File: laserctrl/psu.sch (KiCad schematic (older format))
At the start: 30 parts, among them U1 MC34063

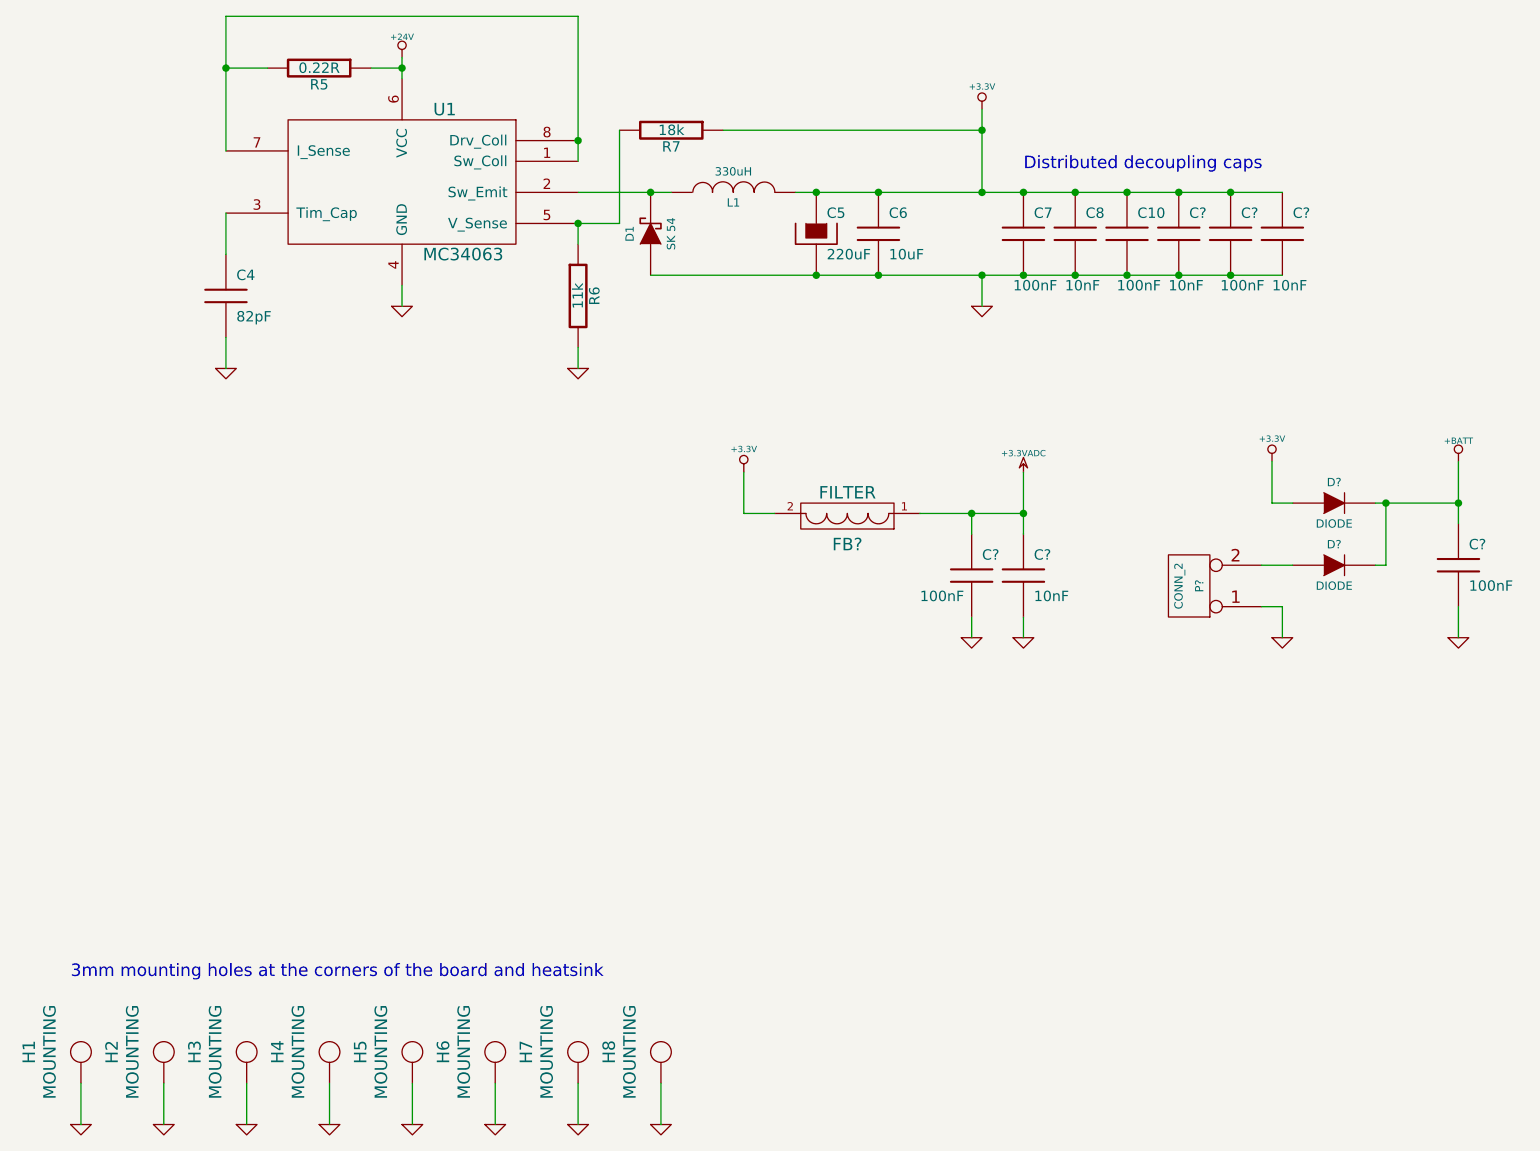
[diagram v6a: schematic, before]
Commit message: Added NTC sensors
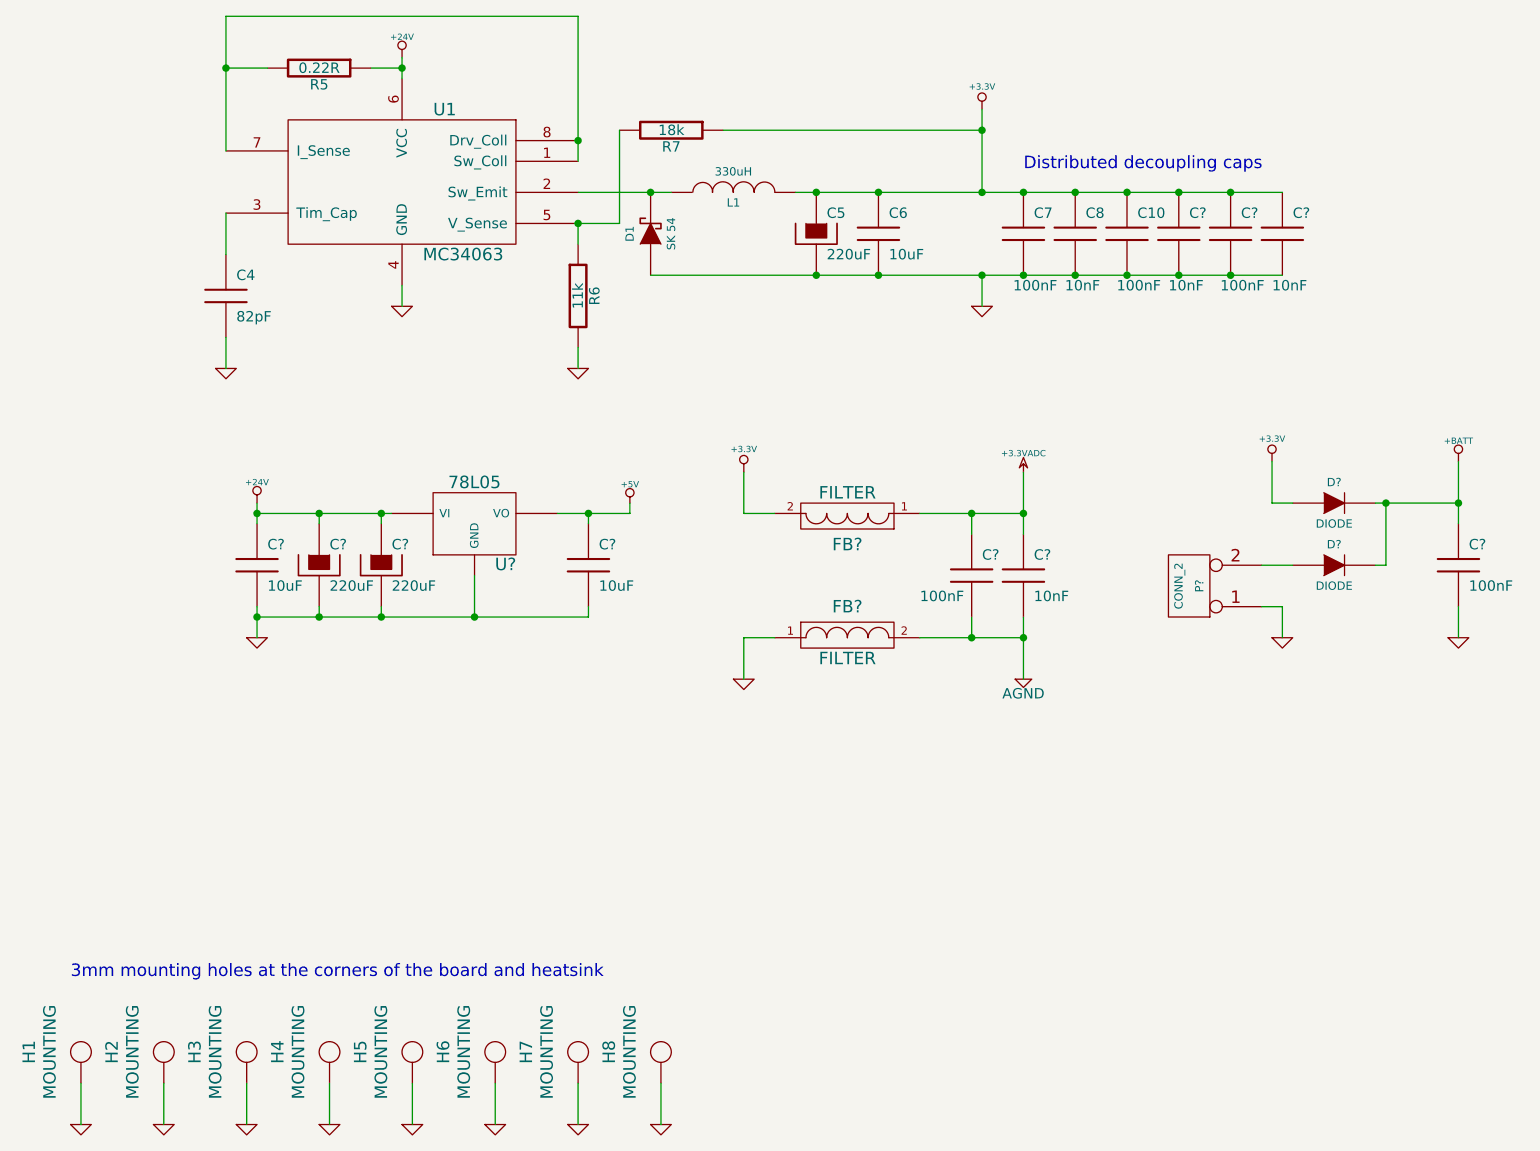
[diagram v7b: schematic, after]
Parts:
- added C? (x2): 10uF, symbol C
- added C? (x2): 220uF, symbol CAPAPOL
- added FB?: FILTER, symbol FILTER
- added U?: 78L05, symbol 78L05
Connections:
- net +24V: now also C?.1, C?.1, C?.1, U?.VI
- net GND: now also C?.2, C?.2, C?.2, C?.2, FB?.1, U?.GND; no longer C?.2, C?.2
- new net +5V: C?.1, U?.VO
- new net AGND: C?.2, C?.2, FB?.2
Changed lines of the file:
@@
-EESchema Schematic File Version 2  date 2011-11-04T21:23:22 CET
+EESchema Schematic File Version 2  date 2011-11-05T15:41:06 CET
 LIBS:power
 LIBS:device
@@
 $Descr A4 11700 8267
 encoding utf-8
-Sheet 6 8
+Sheet 9 9
 Title ""
-Date "4 nov 2011"
+Date "5 nov 2011"
 Rev ""
 Comp ""
@@
 Comment4 ""
 $EndDescr
-Wire Wire Line
-	7200 4600 7300 4600
-Wire Wire Line
-	7300 4600 7300 4750
+$Comp
+L +5V #PWR?
+U 1 1 4EB54A98
+P 4150 4100
+F 0 "#PWR?" H 4150 4190 20  0001 C CNN
+F 1 "+5V" H 4150 4190 30  0000 C CNN
+	1    4150 4100
+	1    0    0    -1
+$EndComp
+Connection ~ 3950 4150
+Wire Wire Line
+	4150 4150 4150 4100
+Wire Wire Line
+	3800 4150 4150 4150
+Connection ~ 3400 4650
+Wire Wire Line
+	3400 4450 3400 4650
+Connection ~ 2950 4650
+Wire Wire Line
+	2950 4600 2950 4650
+Connection ~ 2350 4150
+Wire Wire Line
+	2350 4150 3000 4150
+Connection ~ 2650 4650
+Wire Wire Line
+	2650 4600 2650 4650
+Wire Wire Line
+	2350 4750 2350 4600
+Connection ~ 5800 4750
+Wire Wire Line
+	6050 4750 5550 4750
+Wire Wire Line
+	4850 4750 4700 4750
+Wire Wire Line
+	4700 4750 4700 4950
+Wire Wire Line
+	7200 4400 7350 4400
+Wire Wire Line
+	8150 4750 8150 4600
+Connection ~ 8150 4100
+Wire Wire Line
+	8150 3900 8150 4200
+Wire Wire Line
+	5800 4750 5800 4650
+Connection ~ 5800 4150
+Wire Wire Line
+	6050 4150 5550 4150
+Wire Wire Line
+	4850 4150 4700 4150
+Wire Wire Line
+	4700 4150 4700 3950
+Connection ~ 6800 3000
+Connection ~ 6550 2600
+Connection ~ 6800 2600
+Wire Wire Line
+	4950 2600 7300 2600
+Wire Wire Line
+	3500 7100 3500 6900
+Wire Wire Line
+	4300 7100 4300 6900
+Wire Wire Line
+	3100 6900 3100 7100
+Wire Wire Line
+	2300 6900 2300 7100
+Wire Wire Line
+	1500 6900 1500 7100
+Connection ~ 5850 3000
+Wire Wire Line
+	5850 3000 5850 3150
+Connection ~ 6050 2600
+Connection ~ 6050 3000
+Connection ~ 5850 2300
+Connection ~ 5050 2600
+Wire Wire Line
+	5850 2300 4600 2300
+Connection ~ 4250 2600
+Wire Wire Line
+	3900 2600 4350 2600
+Connection ~ 3900 2750
+Wire Wire Line
+	3900 2850 3900 2750
+Wire Wire Line
+	3900 3350 3900 3450
+Wire Wire Line
+	2200 3300 2200 3450
+Connection ~ 3050 2000
+Wire Wire Line
+	2900 2000 3050 2000
+Connection ~ 3900 2350
+Wire Wire Line
+	3900 2450 3900 1750
+Wire Wire Line
+	3050 2050 3050 1950
+Wire Wire Line
+	2200 2400 2200 1750
+Wire Wire Line
+	2200 1750 3900 1750
+Wire Wire Line
+	2400 2000 2200 2000
+Connection ~ 2200 2000
+Wire Wire Line
+	2200 2900 2200 2700
+Wire Wire Line
+	3050 3050 3050 3150
+Wire Wire Line
+	3900 2750 4100 2750
+Wire Wire Line
+	4100 2750 4100 2300
+Connection ~ 5350 2600
+Connection ~ 5050 3000
+Connection ~ 5350 3000
+Connection ~ 6300 3000
+Connection ~ 6300 2600
+Connection ~ 5850 2600
+Wire Wire Line
+	1900 6900 1900 7100
+Wire Wire Line
+	2700 6900 2700 7100
+Wire Wire Line
+	3900 6900 3900 7100
+Wire Wire Line
+	5850 2200 5850 2600
+Connection ~ 7050 2600
+Connection ~ 6550 3000
+Wire Wire Line
+	7300 3000 4250 3000
+Connection ~ 7050 3000
+Wire Wire Line
+	5800 4150 5800 4250
+Wire Wire Line
+	6050 3950 6050 4250
+Connection ~ 6050 4150
+Wire Wire Line
+	7750 4100 8150 4100
+Wire Wire Line
+	7350 4100 7250 4100
+Wire Wire Line
+	7250 4100 7250 3900
+Wire Wire Line
+	7750 4400 7800 4400
+Wire Wire Line
+	7800 4400 7800 4100
 Connection ~ 7800 4100
 Wire Wire Line
-	7800 4100 7800 4400
-Wire Wire Line
-	7800 4400 7750 4400
-Wire Wire Line
-	7250 3900 7250 4100
-Wire Wire Line
-	7250 4100 7350 4100
-Wire Wire Line
-	7750 4100 8150 4100
-Connection ~ 6050 4150
-Wire Wire Line
-	6050 3950 6050 4250
-Wire Wire Line
-	6050 4650 6050 4750
-Wire Wire Line
-	5800 4150 5800 4250
-Connection ~ 7050 3000
-Wire Wire Line
-	7300 3000 4250 3000
-Connection ~ 6550 3000
-Connection ~ 7050 2600
-Wire Wire Line
-	5850 2200 5850 2600
-Wire Wire Line
-	3900 6900 3900 7100
-Wire Wire Line
-	2700 6900 2700 7100
-Wire Wire Line
-	1900 6900 1900 7100
-Connection ~ 5850 2600
-Connection ~ 6300 2600
-Connection ~ 6300 3000
-Connection ~ 5350 3000
-Connection ~ 5050 3000
-Connection ~ 5350 2600
-Wire Wire Line
-	4100 2300 4100 2750
-Wire Wire Line
-	4100 2750 3900 2750
-Wire Wire Line
-	3050 3050 3050 3150
-Wire Wire Line
-	2200 2900 2200 2700
-Connection ~ 2200 2000
-Wire Wire Line
-	2400 2000 2200 2000
-Wire Wire Line
-	2200 1750 3900 1750
-Wire Wire Line
-	2200 1750 2200 2400
-Wire Wire Line
-	3050 2050 3050 1950
-Wire Wire Line
-	3900 1750 3900 2450
-Connection ~ 3900 2350
-Wire Wire Line
-	2900 2000 3050 2000
-Connection ~ 3050 2000
-Wire Wire Line
-	2200 3300 2200 3450
-Wire Wire Line
-	3900 3350 3900 3450
-Wire Wire Line
-	3900 2750 3900 2850
-Connection ~ 3900 2750
-Wire Wire Line
-	3900 2600 4350 2600
-Connection ~ 4250 2600
-Wire Wire Line
-	5850 2300 4600 2300
-Connection ~ 5050 2600
-Connection ~ 5850 2300
-Connection ~ 6050 3000
-Connection ~ 6050 2600
-Wire Wire Line
-	5850 3000 5850 3150
-Connection ~ 5850 3000
-Wire Wire Line
-	1500 6900 1500 7100
-Wire Wire Line
-	2300 6900 2300 7100
-Wire Wire Line
-	3100 6900 3100 7100
-Wire Wire Line
-	4300 7100 4300 6900
-Wire Wire Line
-	3500 7100 3500 6900
-Wire Wire Line
-	4950 2600 7300 2600
-Connection ~ 6800 2600
-Connection ~ 6550 2600
-Connection ~ 6800 3000
-Wire Wire Line
-	4700 3950 4700 4150
-Wire Wire Line
-	4700 4150 4850 4150
-Wire Wire Line
-	6050 4150 5550 4150
-Connection ~ 5800 4150
-Wire Wire Line
-	5800 4650 5800 4750
-Wire Wire Line
-	8150 3900 8150 4200
-Connection ~ 8150 4100
-Wire Wire Line
-	8150 4750 8150 4600
-Wire Wire Line
-	7200 4400 7350 4400
+	7300 4750 7300 4600
+Wire Wire Line
+	7300 4600 7200 4600
+Wire Wire Line
+	6050 4950 6050 4650
+Connection ~ 6050 4750
+Wire Wire Line
+	2350 4650 3950 4650
+Wire Wire Line
+	3950 4650 3950 4600
+Connection ~ 2350 4650
+Wire Wire Line
+	2350 4100 2350 4200
+Wire Wire Line
+	2650 4200 2650 4150
+Connection ~ 2650 4150
+Wire Wire Line
+	2950 4200 2950 4150
+Connection ~ 2950 4150
+Wire Wire Line
+	3950 4150 3950 4200
+$Comp
+L CAPAPOL C?
+U 1 1 4EB54A69
+P 2950 4400
+F 0 "C?" H 3000 4500 50  0000 L CNN
+F 1 "220uF" H 3000 4300 50  0000 L CNN
+	1    2950 4400
+	1    0    0    -1
+$EndComp
+$Comp
+L CAPAPOL C?
+U 1 1 4EB549F2
+P 2650 4400
+F 0 "C?" H 2700 4500 50  0000 L CNN
+F 1 "220uF" H 2700 4300 50  0000 L CNN
+	1    2650 4400
+	1    0    0    -1
+$EndComp
+$Comp
+L C C?
+U 1 1 4EB5493E
+P 3950 4400
+F 0 "C?" H 4000 4500 50  0000 L CNN
+F 1 "10uF" H 4000 4300 50  0000 L CNN
+	1    3950 4400
+	1    0    0    -1
+$EndComp
+$Comp
+L C C?
+U 1 1 4EB5492E
+P 2350 4400
+F 0 "C?" H 2400 4500 50  0000 L CNN
+F 1 "10uF" H 2400 4300 50  0000 L CNN
+	1    2350 4400
+	1    0    0    -1
+$EndComp
+$Comp
+L GND #PWR?
+U 1 1 4EB54922
+P 2350 4750
+F 0 "#PWR?" H 2350 4750 30  0001 C CNN
+F 1 "GND" H 2350 4680 30  0001 C CNN
+	1    2350 4750
+	1    0    0    -1
+$EndComp
+$Comp
+L +24V #PWR?
+U 1 1 4EB5491D
+P 2350 4100
+F 0 "#PWR?" H 2350 4050 20  0001 C CNN
+F 1 "+24V" H 2350 4200 30  0000 C CNN
+	1    2350 4100
+	1    0    0    -1
+$EndComp
+$Comp
+L 78L05 U?
+U 1 1 4EB54904
+P 3400 4200
+F 0 "U?" H 3550 4004 60  0000 C CNN
+F 1 "78L05" H 3400 4400 60  0000 C CNN
+	1    3400 4200
+	1    0    0    -1
+$EndComp
+$Comp
+L AGND #PWR?
+U 1 1 4EB4727E
+P 6050 4950
+F 0 "#PWR?" H 6050 4950 40  0001 C CNN
+F 1 "AGND" H 6050 4880 50  0000 C CNN
+	1    6050 4950
+	1    0    0    -1
+$EndComp
+$Comp
+L GND #PWR?
+U 1 1 4EB4725D
+P 4700 4950
+F 0 "#PWR?" H 4700 4950 30  0001 C CNN
+F 1 "GND" H 4700 4880 30  0001 C CNN
+	1    4700 4950
+	1    0    0    -1
+$EndComp
+$Comp
+L FILTER FB?
+U 1 1 4EB47252
+P 5200 4750
+F 0 "FB?" H 5200 4900 60  0000 C CNN
+F 1 "FILTER" H 5200 4650 60  0000 C CNN
+	1    5200 4750
+	1    0    0    -1
+$EndComp
 $Comp
 L GND #PWR?
@@
 	1    0    0    -1
 $EndComp
-$Comp
-L GND #PWR?
-U 1 1 4EA3E94A
-P 5800 4750
-F 0 "#PWR?" H 5800 4750 30  0001 C CNN
-F 1 "GND" H 5800 4680 30  0001 C CNN
-	1    5800 4750
-	1    0    0    -1
-$EndComp
-$Comp
-L GND #PWR?
-U 1 1 4EA3E949
-P 6050 4750
-F 0 "#PWR?" H 6050 4750 30  0001 C CNN
-F 1 "GND" H 6050 4680 30  0001 C CNN
-	1    6050 4750
-	1    0    0    -1
-$EndComp

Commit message: Added the chiller and the USB/Serial/ISP/SD subsystems and added some specs on the chiller protocol
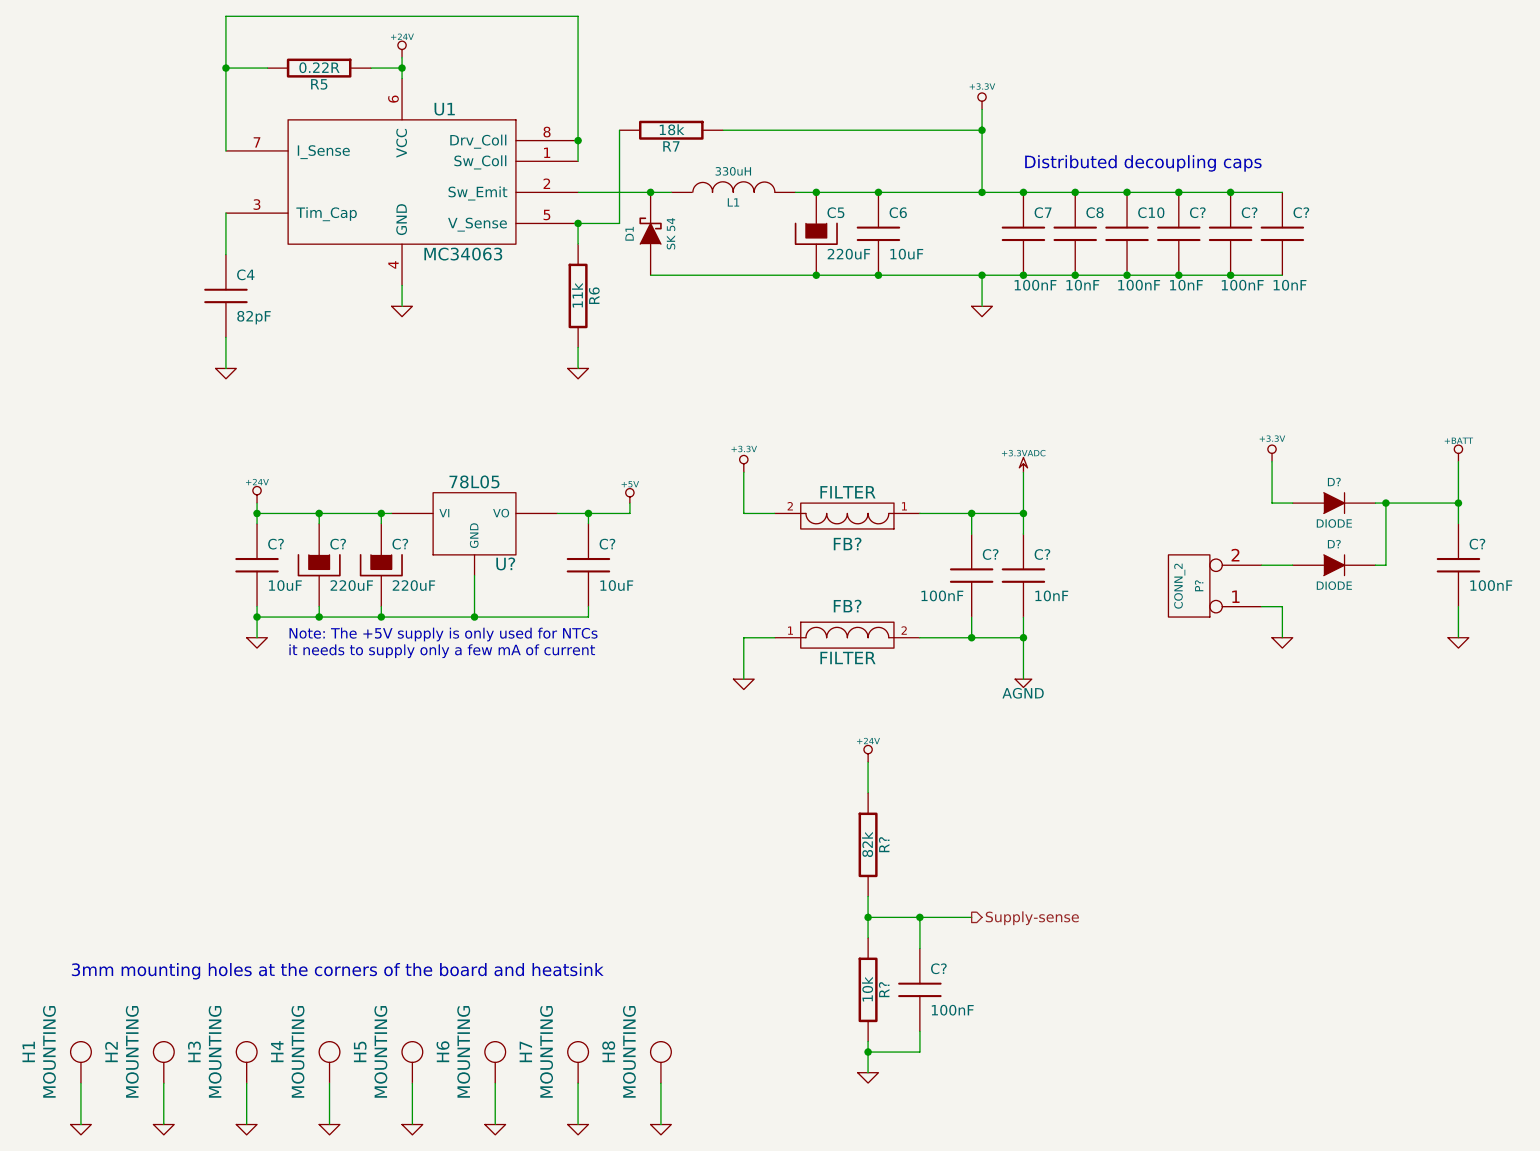
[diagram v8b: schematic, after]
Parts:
- added C?: 100nF, symbol C
- added R?: 82k, symbol R
- added R?: 10k, symbol R
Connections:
- net +24V: now also R?.1
- net GND: now also C?.2, R?.2
- new net Supply-sense: C?.1, R?.1, R?.2
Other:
- note added: "Note: The +5V supply is only used for NTCs\nit needs to supply only a few mA of current"
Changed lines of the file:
@@
-EESchema Schematic File Version 2  date 2011-11-05T15:41:06 CET
+EESchema Schematic File Version 2  date 2011-11-06T20:55:52 CET
 LIBS:power
 LIBS:device
@@
 $Descr A4 11700 8267
 encoding utf-8
-Sheet 9 9
+Sheet 11 11
 Title ""
-Date "5 nov 2011"
+Date "6 nov 2011"
 Rev ""
 Comp ""
@@
 Comment4 ""
 $EndDescr
-$Comp
-L +5V #PWR?
-U 1 1 4EB54A98
-P 4150 4100
-F 0 "#PWR?" H 4150 4190 20  0001 C CNN
-F 1 "+5V" H 4150 4190 30  0000 C CNN
-	1    4150 4100
-	1    0    0    -1
-$EndComp
+Text HLabel 5800 6100 2    50   Output ~ 0
+Supply-sense
+Connection ~ 5550 6100
+Wire Wire Line
+	5800 6100 5300 6100
+Connection ~ 5300 6100
+Wire Wire Line
+	5550 6100 5550 6250
+Wire Wire Line
+	5300 6000 5300 6200
 Connection ~ 3950 4150
 Wire Wire Line
-	4150 4150 4150 4100
-Wire Wire Line
-	3800 4150 4150 4150
+	4150 4100 4150 4150
+Wire Wire Line
+	4150 4150 3800 4150
 Connection ~ 3400 4650
 Wire Wire Line
@@
 Wire Wire Line
 	3950 4150 3950 4200
+Wire Wire Line
+	5300 5350 5300 5500
+Wire Wire Line
+	5300 6700 5300 6850
+Wire Wire Line
+	5550 6650 5550 6750
+Wire Wire Line
+	5550 6750 5300 6750
+Connection ~ 5300 6750
+$Comp
+L C C?
+U 1 1 4EB6CE2C
+P 5550 6450
+F 0 "C?" H 5600 6550 50  0000 L CNN
+F 1 "100nF" H 5600 6350 50  0000 L CNN
+	1    5550 6450
+	1    0    0    -1
+$EndComp
+$Comp
+L +24V #PWR?
+U 1 1 4EB6CE24
+P 5300 5350
+F 0 "#PWR?" H 5300 5300 20  0001 C CNN
+F 1 "+24V" H 5300 5450 30  0000 C CNN
+	1    5300 5350
+	1    0    0    -1
+$EndComp
+$Comp
+L GND #PWR?
+U 1 1 4EB6CE1F
+P 5300 6850
+F 0 "#PWR?" H 5300 6850 30  0001 C CNN
+F 1 "GND" H 5300 6780 30  0001 C CNN
+	1    5300 6850
+	1    0    0    -1
+$EndComp
+$Comp
+L R R?
+U 1 1 4EB6CE1B
+P 5300 6450
+F 0 "R?" V 5380 6450 50  0000 C CNN
+F 1 "10k" V 5300 6450 50  0000 C CNN
+	1    5300 6450
+	1    0    0    -1
+$EndComp
+$Comp
+L R R?
+U 1 1 4EB6CE16
+P 5300 5750
+F 0 "R?" V 5380 5750 50  0000 C CNN
+F 1 "82k" V 5300 5750 50  0000 C CNN
+	1    5300 5750
+	1    0    0    -1
+$EndComp
+Text Notes 2500 4850 0    50   ~ 0
+Note: The +5V supply is only used for NTCs\nit needs to supply only a few mA of current
+$Comp
+L +5V #PWR?
+U 1 1 4EB54A98
+P 4150 4100
+F 0 "#PWR?" H 4150 4190 20  0001 C CNN
+F 1 "+5V" H 4150 4190 30  0000 C CNN
+	1    4150 4100
+	1    0    0    -1
+$EndComp
 $Comp
 L CAPAPOL C?
